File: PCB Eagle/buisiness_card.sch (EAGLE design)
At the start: 24 parts, among them Y1 16MHz

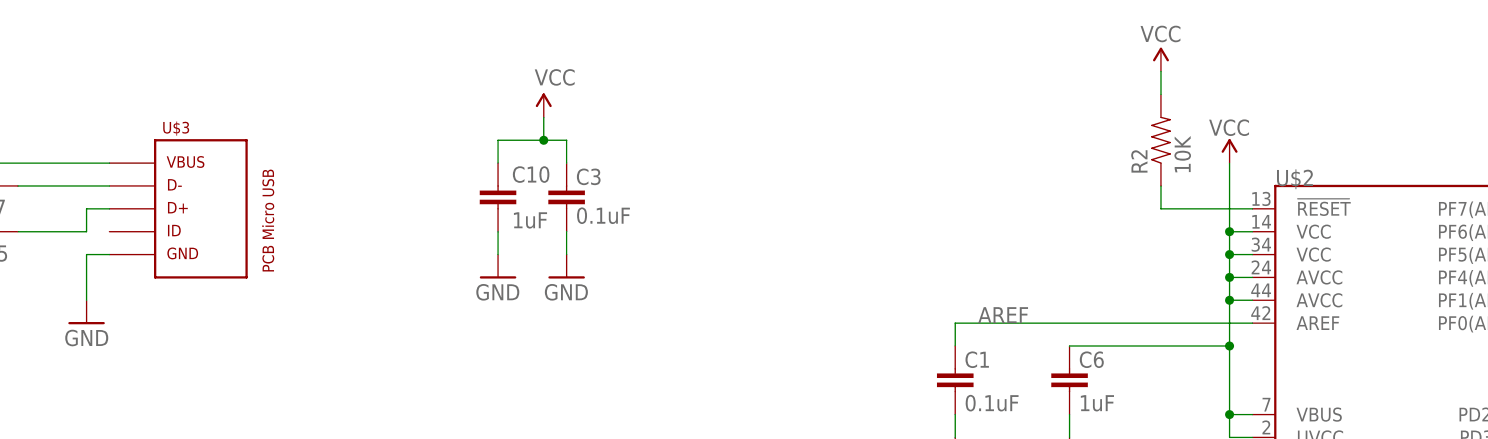
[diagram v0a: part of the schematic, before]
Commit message: Added BOM and updated components references.
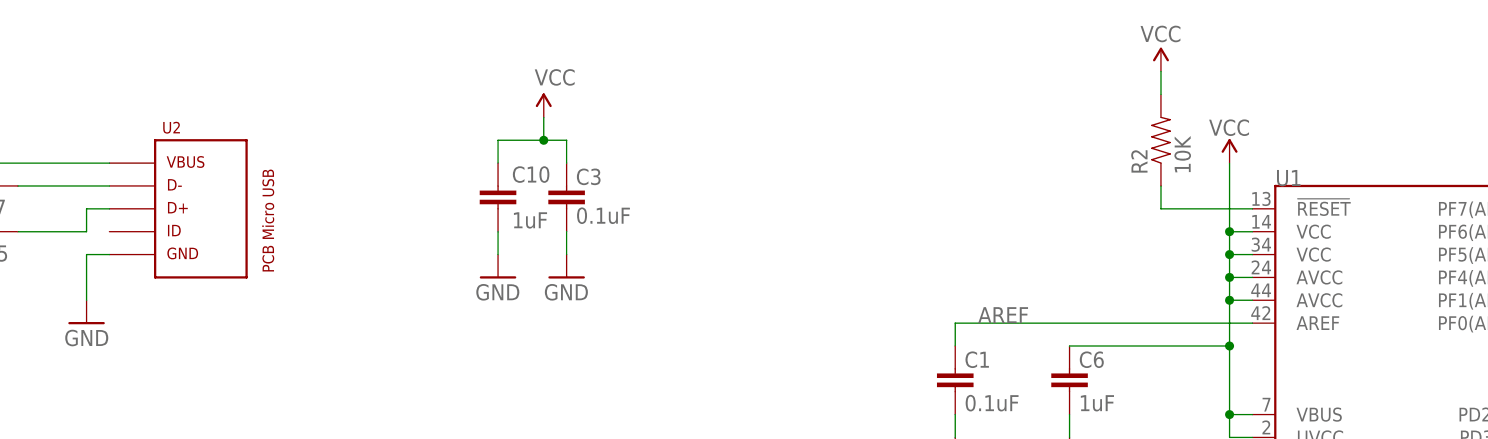
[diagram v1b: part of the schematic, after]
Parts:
- renumbered U$10 to B8, U$11 to B7, U$12 to B10, U$13 to B9, U$2 to U1, U$3 to U2, U$4 to B4, U$5 to B1, U$6 to B2, U$7 to B3, U$8 to B6, U$9 to B5
